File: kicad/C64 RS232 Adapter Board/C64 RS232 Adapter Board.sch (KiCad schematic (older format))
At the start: 29 parts, among them J1 RS232_HDR, J2 DB25_RS232, J3 C64_USER_PORT, J4 User Port Breakout, SW1 RESET, U1 MAX3241ECAI+T

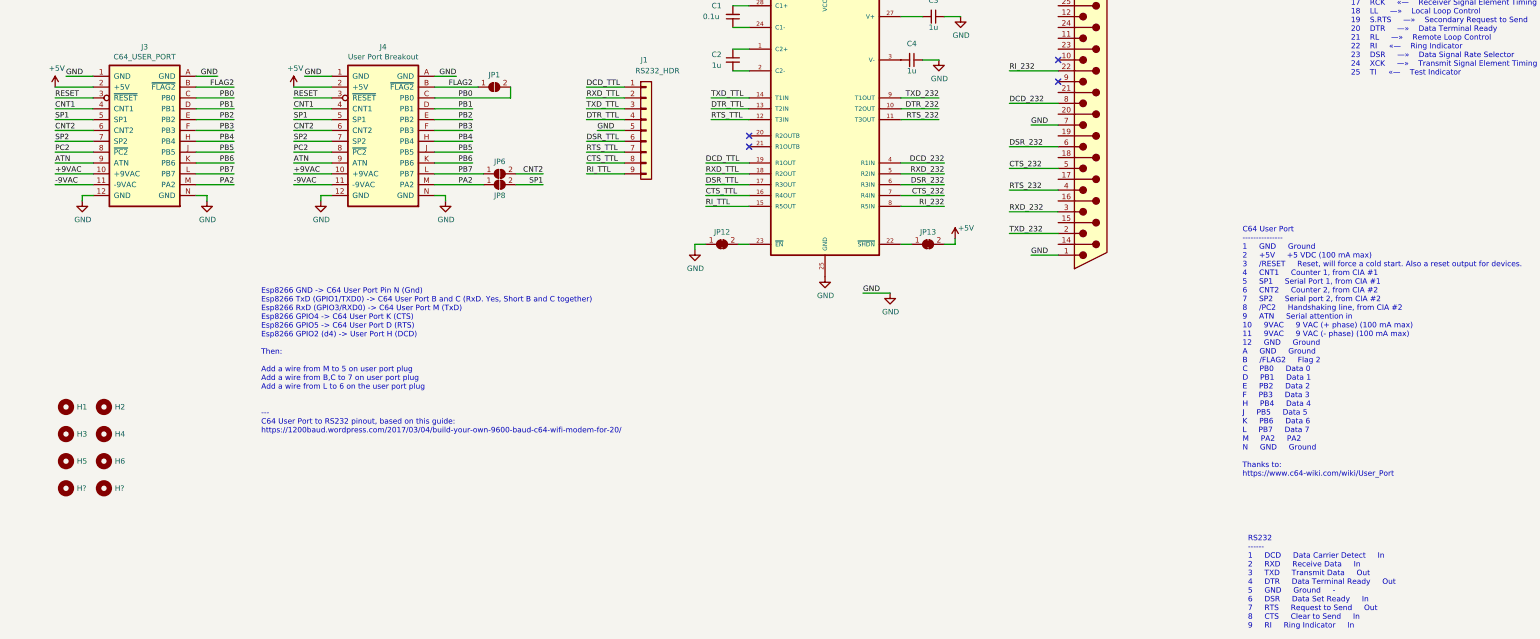
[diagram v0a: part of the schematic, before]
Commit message: moved pinouts around
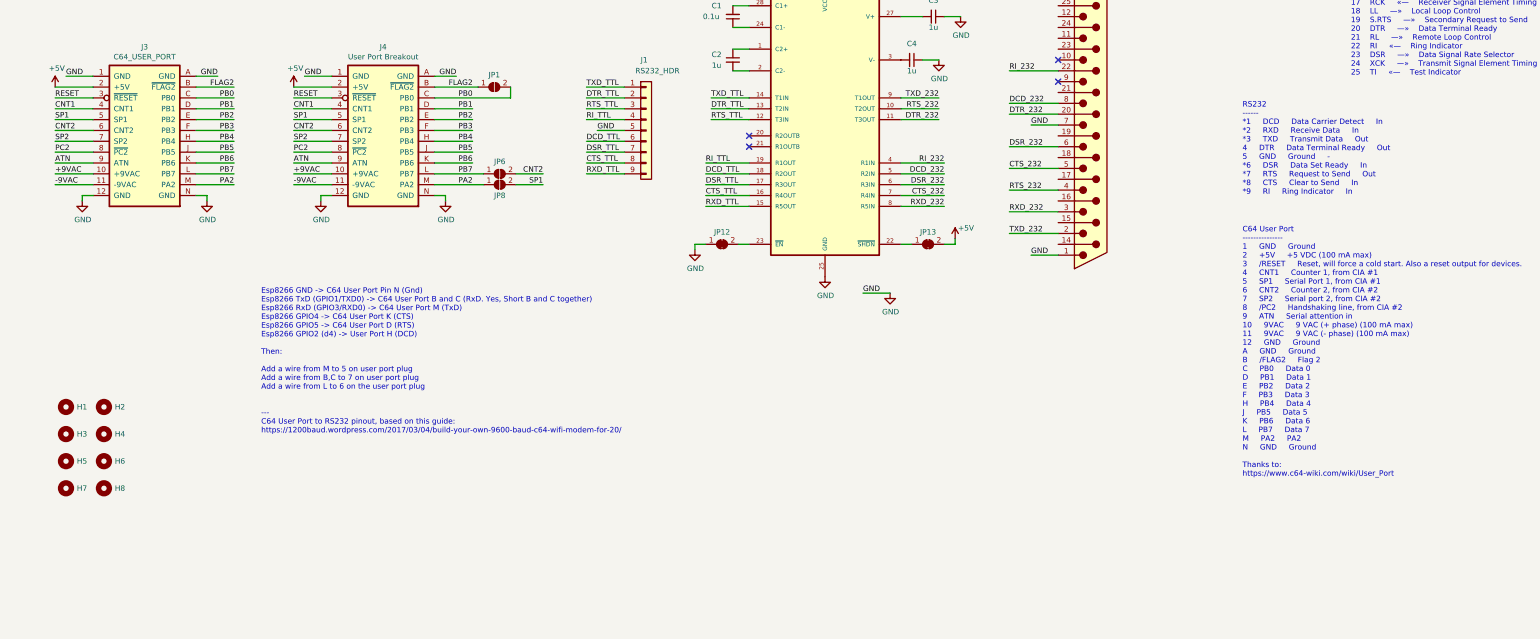
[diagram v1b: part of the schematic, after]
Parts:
- gave numbers to parts that had none: 2
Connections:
- net DCD_232: now also U1.5 (R2IN); no longer U1.4 (R1IN)
- net DCD_TTL: now also J1.6 (Pin_6), U1.18 (R2OUT); no longer J1.1 (Pin_1), U1.19 (R1OUT)
- net DSR_TTL: now also J1.7 (Pin_7); no longer J1.6 (Pin_6)
- net DTR_232: now also J2.20 (P20), U1.11 (T3OUT); no longer U1.10 (T2OUT)
- net DTR_TTL: now also J1.2 (Pin_2); no longer J1.4 (Pin_4)
- net RI_232: now also U1.4 (R1IN); no longer U1.8 (R5IN)
- net RI_TTL: now also J1.4 (Pin_4), U1.19 (R1OUT); no longer J1.9 (Pin_9), U1.15 (R5OUT)
- net RTS_232: now also U1.10 (T2OUT); no longer U1.11 (T3OUT)
- net RTS_TTL: now also J1.3 (Pin_3); no longer J1.7 (Pin_7)
- net RXD_232: now also U1.8 (R5IN); no longer U1.5 (R2IN)
- net RXD_TTL: now also J1.9 (Pin_9), U1.15 (R5OUT); no longer J1.2 (Pin_2), U1.18 (R2OUT)
- net TXD_TTL: now also J1.1 (Pin_1); no longer J1.3 (Pin_3)
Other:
- note added: "RS232\n------\n*1 DCD Data Carrier Detect In\n*2 RXD Receive Data In\n*3 TXD Transmit Data Out\n4 DTR Data Terminal Ready Out\n5 GND Ground -\n*6 DSR Data Set Ready In\n*7 RTS Request to Send Out\n*8 CTS Clear to Send In\n*9 RI Ring Indicator In"
- note removed: "RS232\n------\n1 DCD Data Carrier Detect In\n2 RXD Receive Data In\n3 TXD Transmit Data Out\n4 DTR Data Terminal Ready Out\n5 GND Ground -\n6 DSR Data Set Ready In\n7 RTS Request to Send Out\n8 CTS Clear to Send In\n9 RI Ring Indicator In"
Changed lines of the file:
@@
 Text Notes 11900 6550 0    50   ~ 0
 C64 User Port\n---------------\n1 	GND 	Ground\n2 	+5V 	+5 VDC (100 mA max)\n3 	/RESET 	Reset, will force a cold start. Also a reset output for devices.\n4 	CNT1 	Counter 1, from CIA #1\n5 	SP1 	Serial Port 1, from CIA #1\n6 	CNT2 	Counter 2, from CIA #2\n7 	SP2 	Serial port 2, from CIA #2\n8 	/PC2 	Handshaking line, from CIA #2\n9 	ATN 	Serial attention in\n10 	9VAC 	9 VAC (+ phase) (100 mA max)\n11 	9VAC 	9 VAC (- phase) (100 mA max)\n12 	GND 	Ground\nA 	GND 	Ground\nB 	/FLAG2 	Flag 2\nC 	PB0 	Data 0\nD 	PB1 	Data 1\nE 	PB2 	Data 2\nF 	PB3 	Data 3\nH 	PB4 	Data 4\nJ 	PB5 	Data 5\nK 	PB6 	Data 6\nL 	PB7 	Data 7\nM 	PA2 	PA2\nN 	GND 	Ground \n\nThanks to:\nhttps://www.c64-wiki.com/wiki/User_Port
-Text Notes 11950 7950 0    50   ~ 0
-RS232\n------\n1 	DCD 	Data Carrier Detect 	In\n2 	RXD 	Receive Data 	In\n3 	TXD 	Transmit Data 	Out\n4 	DTR 	Data Terminal Ready 	Out\n5 	GND 	Ground 	-\n6 	DSR 	Data Set Ready 	In\n7 	RTS 	Request to Send 	Out\n8 	CTS 	Clear to Send 	In\n9 	RI 	Ring Indicator 	In
+Text Notes 11900 3950 0    50   ~ 0
+RS232\n------\n*1 	DCD 	Data Carrier Detect 	In\n*2 	RXD 	Receive Data 	In\n*3 	TXD 	Transmit Data 	Out\n4 	DTR 	Data Terminal Ready 	Out\n5 	GND 	Ground 	-\n*6 	DSR 	Data Set Ready 	In\n*7 	RTS 	Request to Send 	Out\n*8 	CTS 	Clear to Send 	In\n*9 	RI 	Ring Indicator 	In
 $Comp
 L Connector:DB25_Male J2
@@
 Wire Wire Line
 	9250 4400 9250 4350
-Text Label 9150 3650 2    50   ~ 0
+Text Label 9150 3750 2    50   ~ 0
 DCD_232
-Text Label 9150 3750 2    50   ~ 0
+Text Label 9150 4050 2    50   ~ 0
 RXD_232
 Text Label 9150 3850 2    50   ~ 0
@@
 Text Label 9150 3950 2    50   ~ 0
 CTS_232
-Text Label 9150 4050 2    50   ~ 0
+Text Label 9150 3650 2    50   ~ 0
 RI_232
 Text Label 9100 3050 2    50   ~ 0
 TXD_232
+Text Label 9100 3250 2    50   ~ 0
+DTR_232
 Text Label 9100 3150 2    50   ~ 0
-DTR_232
-Text Label 9100 3250 2    50   ~ 0
 RTS_232
 Wire Wire Line
@@
 Wire Wire Line
 	8750 4050 9150 4050
-Text Label 6950 3650 0    50   ~ 0
-DCD_TTL
-Text Label 6950 3750 0    50   ~ 0
+Text Label 6950 4050 0    50   ~ 0
 RXD_TTL
 Text Label 6950 3850 0    50   ~ 0
@@
 Text Label 6950 3950 0    50   ~ 0
 CTS_TTL
-Text Label 6950 4050 0    50   ~ 0
+Text Label 6950 3650 0    50   ~ 0
 RI_TTL
 $Comp
@@
 Text Label 5950 3350 0    50   ~ 0
 GND
-Text Label 5850 3750 0    50   ~ 0
+Text Label 5850 3250 0    50   ~ 0
 RI_TTL
 Text Label 5850 3650 0    50   ~ 0
 CTS_TTL
+Text Label 5850 3150 0    50   ~ 0
+RTS_TTL
 Text Label 5850 3550 0    50   ~ 0
-RTS_TTL
+DSR_TTL
+Text Label 5850 3750 0    50   ~ 0
+RXD_TTL
 Text Label 5850 3450 0    50   ~ 0
-DSR_TTL
+DCD_TTL
+Text Label 5850 2950 0    50   ~ 0
+TXD_TTL
+Wire Wire Line
+	7000 3050 7350 3050
+Wire Wire Line
+	7000 3250 7350 3250
+Wire Wire Line
+	6950 3850 7350 3850
+Wire Wire Line
+	6950 4050 7350 4050
+Wire Wire Line
+	6200 3250 5850 3250
 Text Label 5850 3050 0    50   ~ 0
-RXD_TTL
-Text Label 5850 2950 0    50   ~ 0
-DCD_TTL
-Text Label 5850 3150 0    50   ~ 0
-TXD_TTL
-Wire Wire Line
-	7000 3050 7350 3050
-Wire Wire Line
-	7000 3250 7350 3250
-Wire Wire Line
-	6950 3850 7350 3850
-Wire Wire Line
-	6950 4050 7350 4050
-Wire Wire Line
-	6200 3250 5850 3250
-Text Label 5850 3250 0    50   ~ 0
 DTR_TTL
 Text Notes -3000 3650 0    50   ~ 0
@@
 $EndComp
 $Comp
-L Mechanical:MountingHole H?
+L Mechanical:MountingHole H7
 U 1 1 5F29F7DC
 P 1050 6650
-F 0 "H?" H 1150 6650 50  0000 L CNN
+F 0 "H7" H 1150 6650 50  0000 L CNN
 F 1 "MountingHole" H 1150 6605 50  0001 L CNN
 F 2 "MountingHole:MountingHole_2.5mm" H 1050 6650 50  0001 C CNN
@@
 $EndComp
 $Comp
-L Mechanical:MountingHole H?
+L Mechanical:MountingHole H8
 U 1 1 5F29FB17
 P 1400 6650
-F 0 "H?" H 1500 6650 50  0000 L CNN
+F 0 "H8" H 1500 6650 50  0000 L CNN
 F 1 "MountingHole" H 1500 6605 50  0001 L CNN
 F 2 "MountingHole:MountingHole_2.5mm" H 1400 6650 50  0001 C CNN
@@
 	1    0    0    -1
 $EndComp
+Wire Wire Line
+	10200 3200 9750 3200
+Text Label 9750 3200 0    50   ~ 0
+DTR_232
+Text Label 6950 3750 0    50   ~ 0
+DCD_TTL
 $EndSCHEMATC

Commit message: 232 signals routed clean
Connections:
- net CTS_232: now also U1.5 (R2IN); no longer U1.7 (R4IN)
- net CTS_TTL: now also U1.18 (R2OUT); no longer U1.16 (R4OUT)
- net DCD_232: now also U1.7 (R4IN); no longer U1.5 (R2IN)
- net DCD_TTL: now also U1.16 (R4OUT); no longer U1.18 (R2OUT)
- net RI_232: now also U1.8 (R5IN); no longer U1.4 (R1IN)
- net RI_TTL: now also U1.15 (R5OUT); no longer U1.19 (R1OUT)
- net RXD_232: now also U1.4 (R1IN); no longer U1.8 (R5IN)
- net RXD_TTL: now also U1.19 (R1OUT); no longer U1.15 (R5OUT)
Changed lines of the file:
@@
 Wire Wire Line
 	9250 4400 9250 4350
-Text Label 9150 3750 2    50   ~ 0
+Text Label 9150 3950 2    50   ~ 0
 DCD_232
-Text Label 9150 4050 2    50   ~ 0
+Text Label 9150 3650 2    50   ~ 0
 RXD_232
 Text Label 9150 3850 2    50   ~ 0
@@
 Text Label 7000 3250 0    50   ~ 0
 RTS_TTL
-Text Label 9150 3950 2    50   ~ 0
+Text Label 9150 3750 2    50   ~ 0
 CTS_232
-Text Label 9150 3650 2    50   ~ 0
+Text Label 9150 4050 2    50   ~ 0
 RI_232
 Text Label 9100 3050 2    50   ~ 0
@@
 Wire Wire Line
 	8750 4050 9150 4050
-Text Label 6950 4050 0    50   ~ 0
+Text Label 6950 3650 0    50   ~ 0
 RXD_TTL
 Text Label 6950 3850 0    50   ~ 0
 DSR_TTL
-Text Label 6950 3950 0    50   ~ 0
+Text Label 6950 3750 0    50   ~ 0
 CTS_TTL
-Text Label 6950 3650 0    50   ~ 0
+Text Label 6950 4050 0    50   ~ 0
 RI_TTL
 $Comp
@@
 Text Label 9750 3200 0    50   ~ 0
 DTR_232
-Text Label 6950 3750 0    50   ~ 0
+Text Label 6950 3950 0    50   ~ 0
 DCD_TTL
 $EndSCHEMATC

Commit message: First layout done
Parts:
- J1: symbol Connector_Generic:Conn_01x09 -> Connector_Generic:Conn_01x10
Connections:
- net +5V: now also J1.10 (Pin_10)
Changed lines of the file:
@@
 RI_TTL
 $Comp
-L Connector_Generic:Conn_01x09 J1
+L Connector_Generic:Conn_01x10 J1
 U 1 1 5F1A3DF6
 P 6400 3350
@@
 Text Label 6950 3950 0    50   ~ 0
 DCD_TTL
+Wire Wire Line
+	6200 3850 5950 3850
+$Comp
+L power:+5V #PWR?
+U 1 1 5F3D8503
+P 5950 3850
+F 0 "#PWR?" H 5950 3700 50  0001 C CNN
+F 1 "+5V" H 5965 4023 50  0000 C CNN
+F 2 "" H 5950 3850 50  0001 C CNN
+F 3 "" H 5950 3850 50  0001 C CNN
+	1    5950 3850
+	0    -1   -1   0
+$EndComp
 $EndSCHEMATC

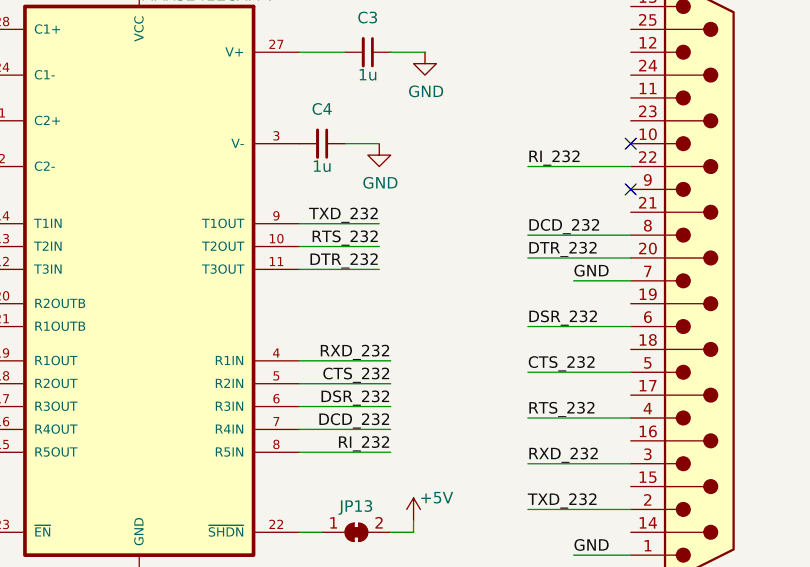
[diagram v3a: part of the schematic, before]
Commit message: removed 3d files
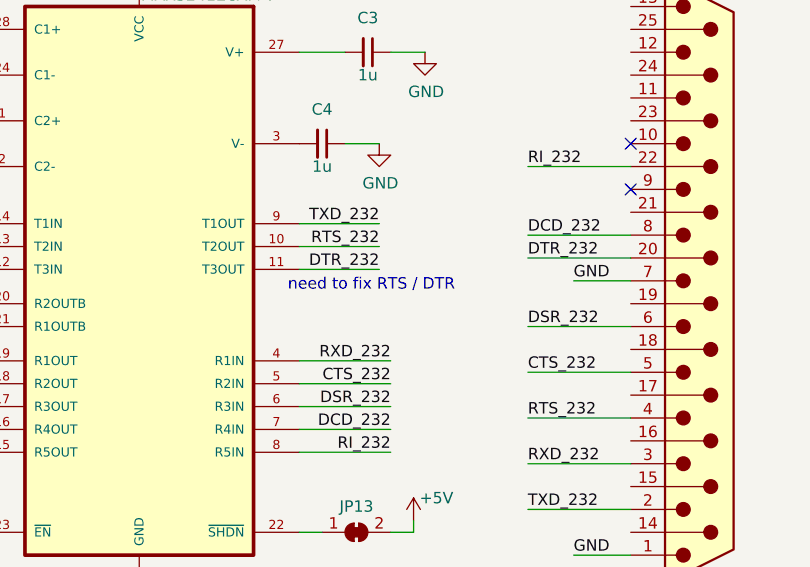
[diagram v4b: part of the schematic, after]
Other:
- note added: "need to fix RTS / DTR"
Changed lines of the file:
@@
 	0    -1   -1   0
 $EndComp
+Text Notes 8700 3350 0    50   ~ 0
+need to fix RTS / DTR
 $EndSCHEMATC
